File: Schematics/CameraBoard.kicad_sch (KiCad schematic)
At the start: 0 parts

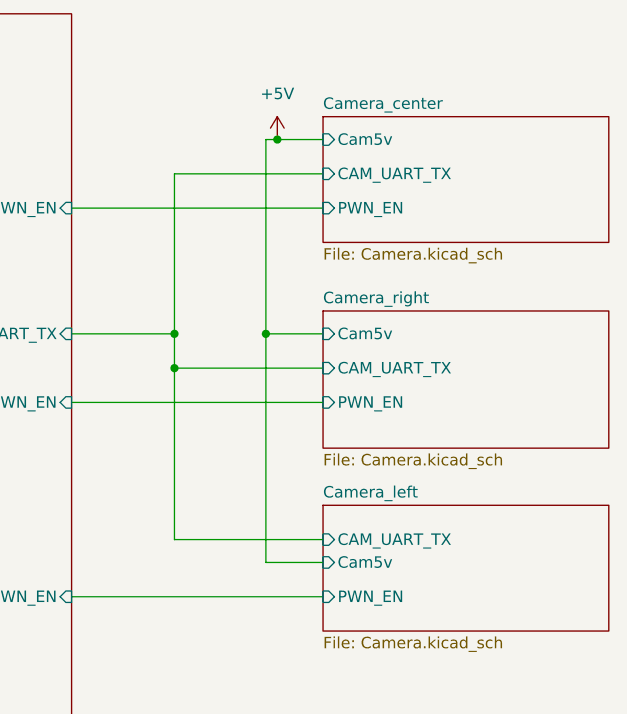
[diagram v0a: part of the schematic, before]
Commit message: dfm complete sent for order
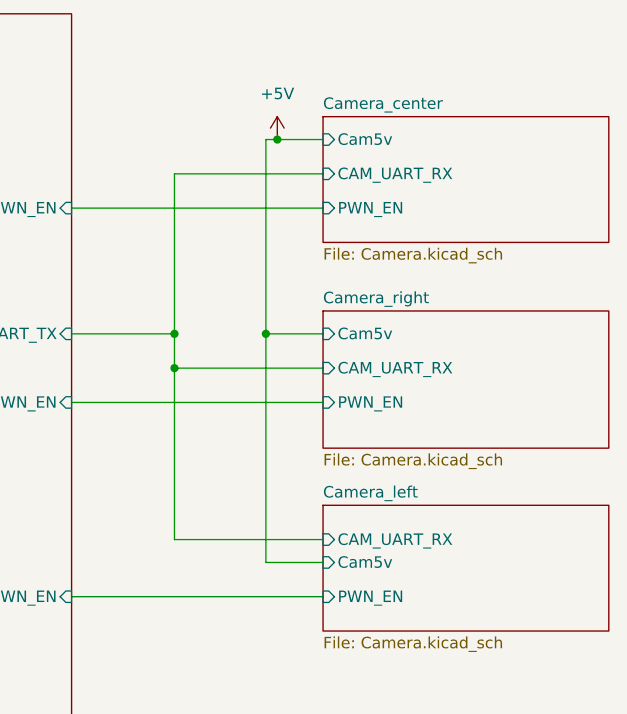
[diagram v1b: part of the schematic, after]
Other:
- sheet Camera_center ports: added CAM_UART_RX; removed CAM_UART_TX
- sheet Camera_left ports: added CAM_UART_RX; removed CAM_UART_TX
- sheet Camera_right ports: added CAM_UART_RX; removed CAM_UART_TX
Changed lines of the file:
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@@
-			)
-		)
-		(pin "CAM_UART_TX" input
-			(at 191.77 64.77 180)
-			(effects
-				(font
-					(size 1.27 1.27)
-				)
-				(justify left)
 			)
 		)
@@
 			)
 		)
+		(pin "CAM_UART_RX" input
+			(at 191.77 64.77 180)
+			(effects
+				(font
+					(size 1.27 1.27)
+				)
+				(justify left)
+			)
+		)
 		(instances
 			(project "CameraBoard"
@@
 			)
 		)
-		(pin "CAM_UART_TX" input
-			(at 191.77 86.36 180)
-			(effects
-				(font
-					(size 1.27 1.27)
-				)
-				(justify left)
-			)
-		)
 		(pin "Cam5v" input
 			(at 191.77 82.55 180)
@@
 			)
 		)
+		(pin "CAM_UART_RX" input
+			(at 191.77 86.36 180)
+			(effects
+				(font
+					(size 1.27 1.27)
+				)
+				(justify left)
+			)
+		)
 		(instances
 			(project "CameraBoard"
@@
 			)
 		)
-		(pin "CAM_UART_TX" input
-			(at 191.77 105.41 180)
-			(effects
-				(font
-					(size 1.27 1.27)
-				)
-				(justify left)
-			)
-		)
 		(pin "Cam5v" input
 			(at 191.77 107.95 180)
 			(effects
 				(font
+					(size 1.27 1.27)
+				)
+				(justify left)
+			)
+		)
+		(pin "CAM_UART_RX" input
+			(at 191.77 105.41 180)
+			(effects
+				(font
